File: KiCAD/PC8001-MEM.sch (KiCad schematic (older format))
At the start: 30 parts, among them J1 PC-8001 ext BUS, U1 74LS30, U10 74LS148, U11 628128, U2 74LS02, U3 74LS05, U4 74LS32, U5 74LS32, U6 74LS273, U7 74LS541, U8 74LS540, U9 74LS148

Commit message: README追加
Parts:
- removed C10, C11, C9: 0.1u, Capacitor_THT:C_Disc_D3.0mm_W1.6mm_P2.50mm, symbol Device:C
- removed R1, R2: 10k, symbol Device:R_US
- removed U1: 74LS30, symbol 74xx:74LS30
- removed U10, U9: 74LS148, symbol 74xx:74LS148
- removed U2: 74LS02, symbol 74xx:74LS02
- removed U3: 74LS05, symbol 74xx:74LS05
- removed U5: 74LS32, symbol 74xx:74LS32
- removed U8: 74LS540, symbol 74xx:74LS540
- added C? (x2): 0.1u, Capacitor_THT:C_Disc_D3.0mm_W1.6mm_P2.50mm, symbol Device:C
- added U? (x2): 74LS138, symbol 74xx:74LS138
- added U? (x3): 74LS74, symbol 74xx:74LS74
- added U? (x5): 74LS32, symbol 74xx:74LS32
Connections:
- net labels added: E2#RD, E2#WR, E3#RD, E3#WR, ~RAMRD, ~RAMWR
- net labels removed: 1MCS2, MA15, MA16, ~IOE2
- wire segments 345 -> 264
- no-connect marks 21 -> 25
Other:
- note added: "$010 - 02 : $E2 WR\n$100 - 04 : $E2 RD\n$011 - 03 : $E3 WR\n$101 - 05 : $E3 RD\n"
- note removed: "I/O E2h"
- moved on the sheet: C1, C12, C2, C3, C4, C5, C6, C7, C8, J1, MH1, MH2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

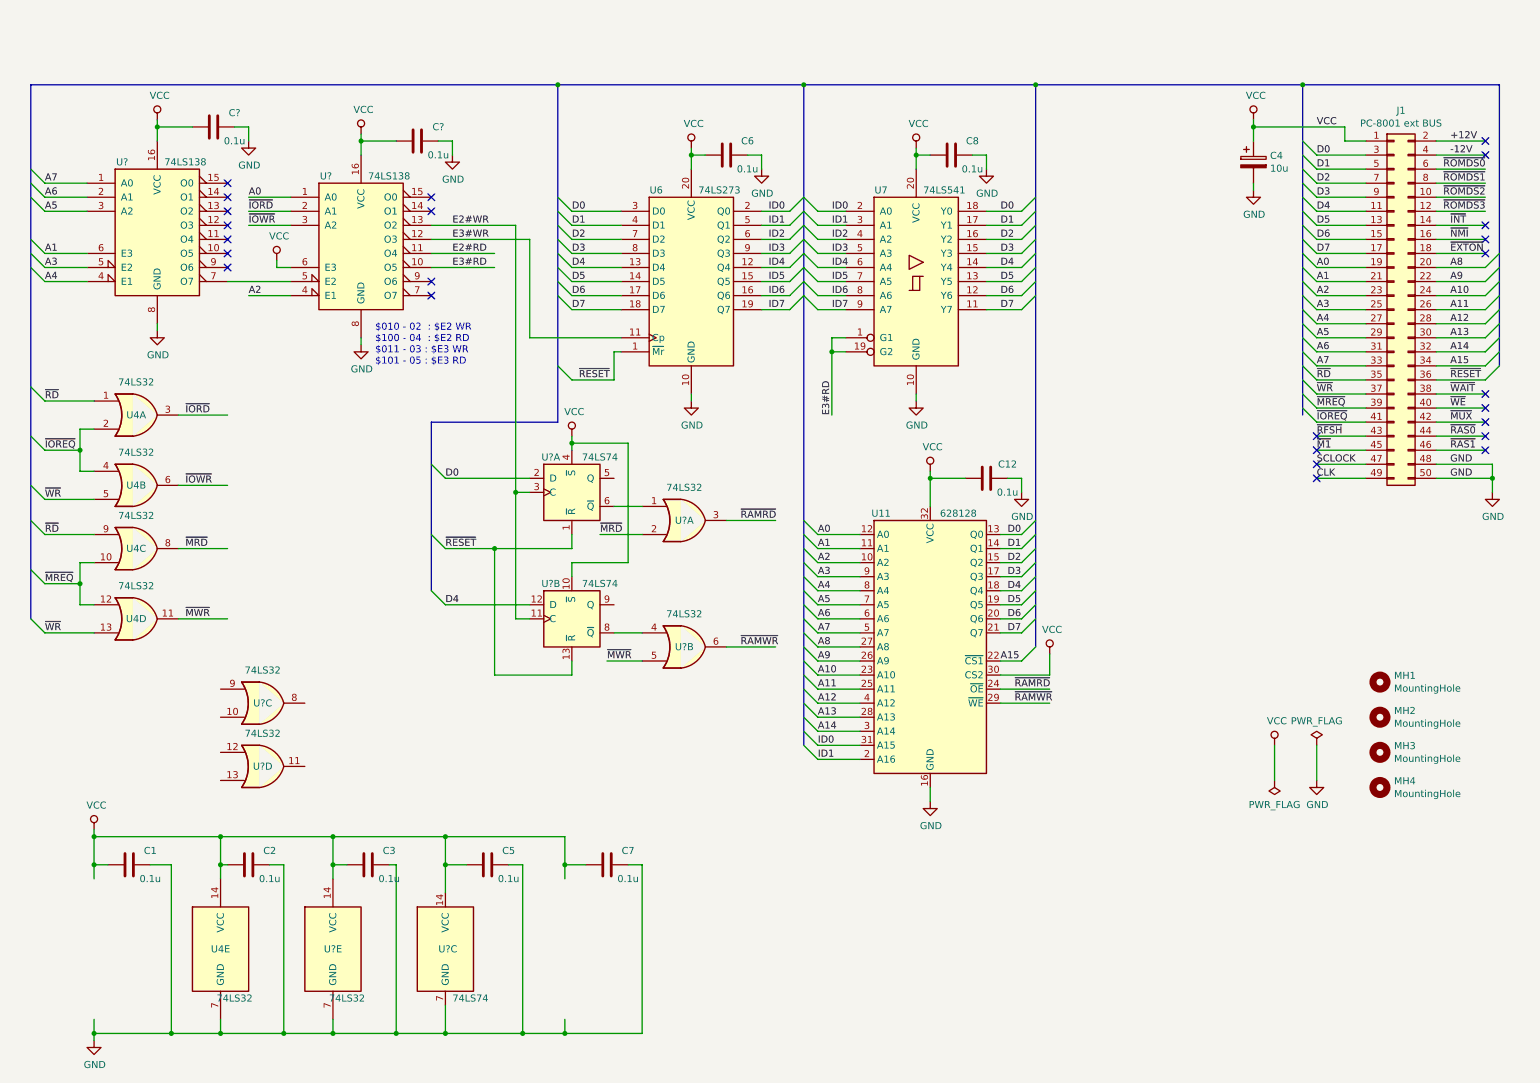
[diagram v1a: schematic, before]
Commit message: 回路図修正、イメージ追加
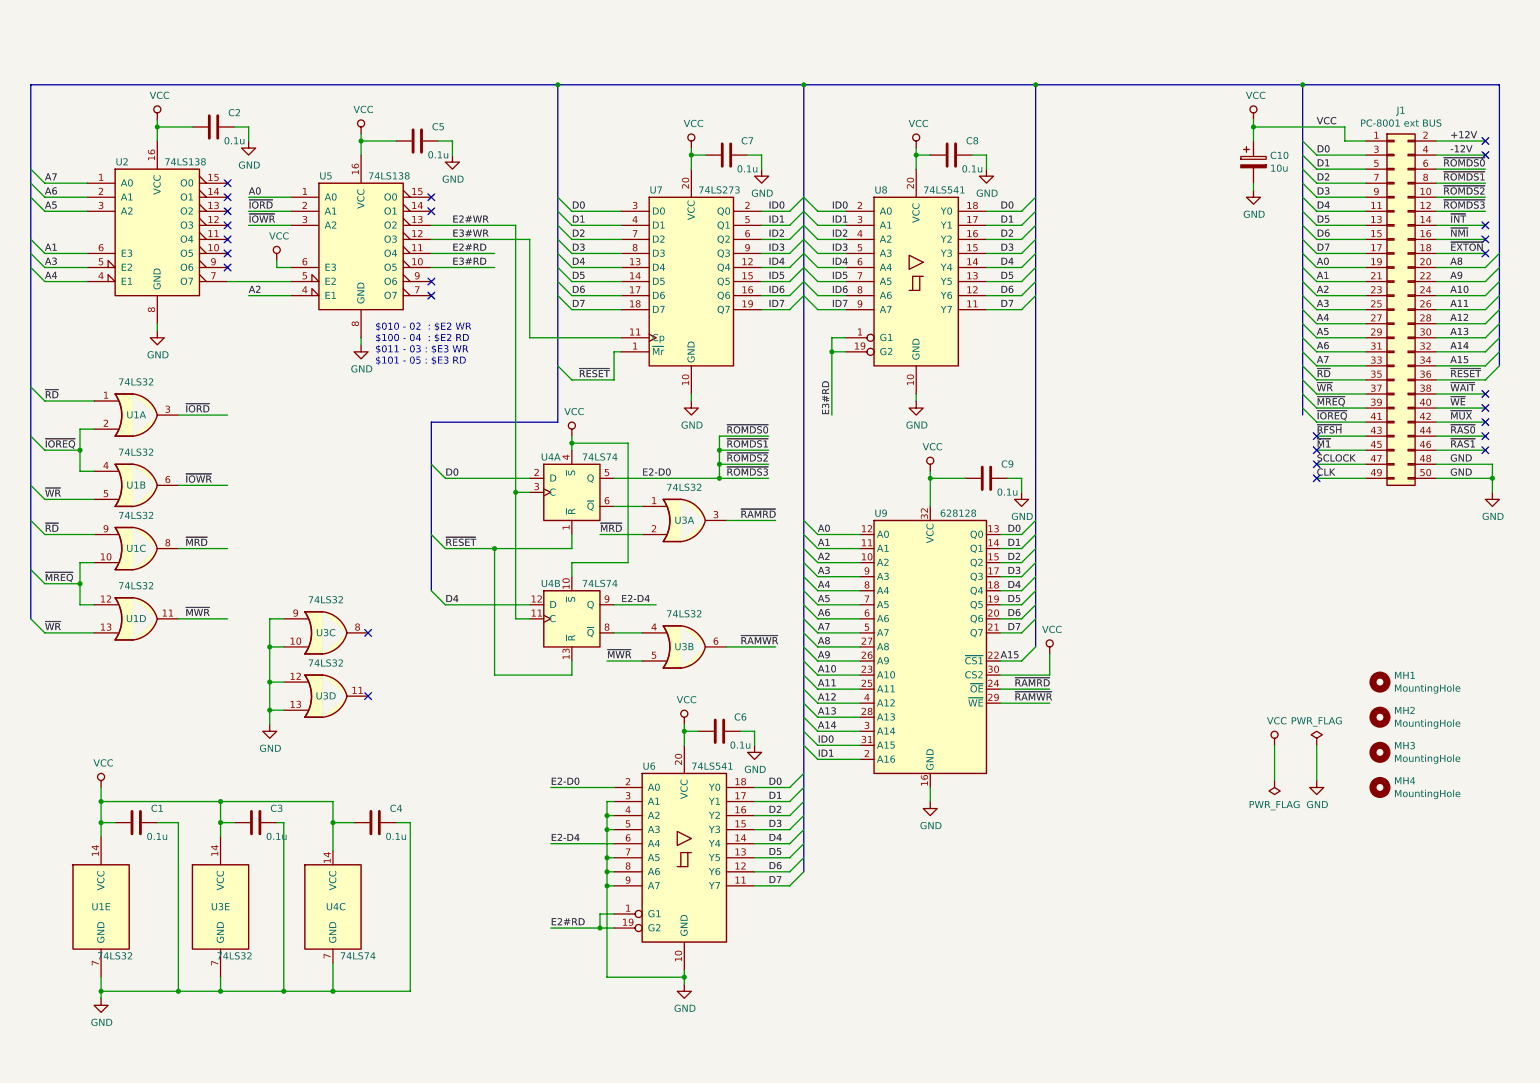
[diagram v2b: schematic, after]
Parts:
- removed C2, C7: 0.1u, Capacitor_THT:C_Disc_D3.0mm_W1.6mm_P2.50mm, symbol Device:C
- added C6: 0.1u, Capacitor_THT:C_Disc_D3.0mm_W1.6mm_P2.50mm, symbol Device:C
- added U6: 74LS541, symbol 74xx:74LS541
- gave numbers to parts that had none: 6
- renumbered C4 to C10, C5 to C4, C6 to C7, C12 to C9, U4 to U1, U6 to U7, U7 to U8, U11 to U9
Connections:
- net labels added: E2-D0, E2-D4
- wire segments 264 -> 297
- no-connect marks 25 -> 27
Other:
- moved on the sheet: C1, C3, C4, U1E, U3C, U3D, U3E, U4C

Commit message: アドレス E2用 LED追加
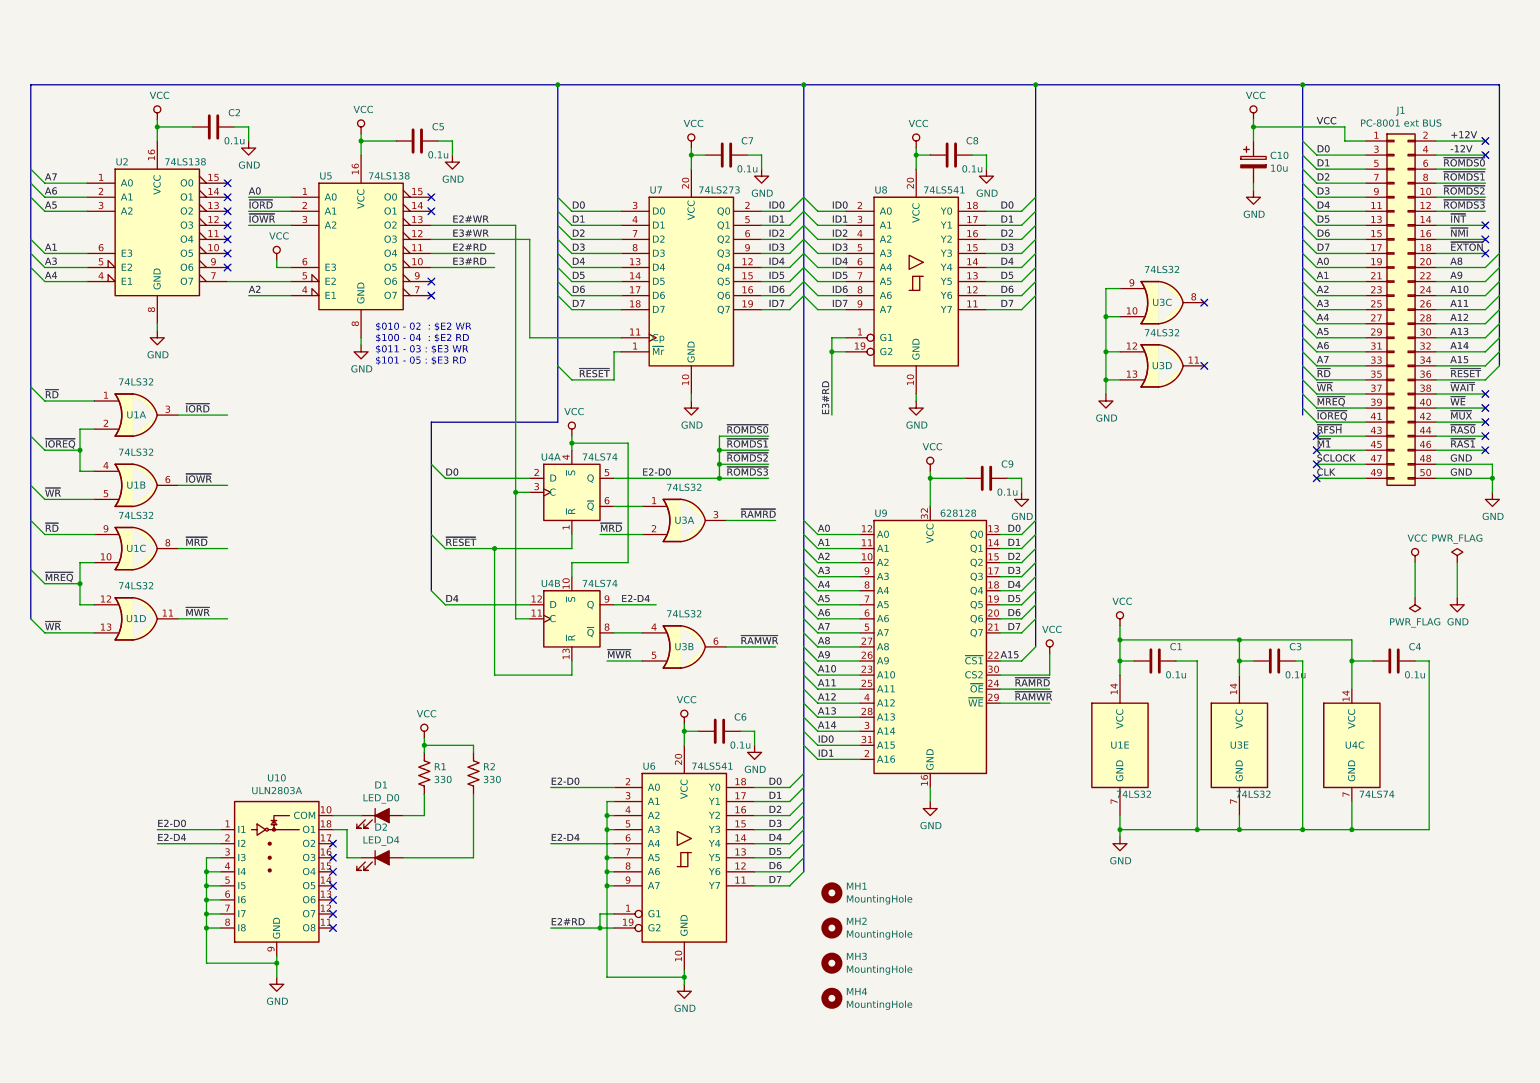
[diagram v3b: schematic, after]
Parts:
- added D1: LED_D0, symbol Device:LED_ALT
- added D2: LED_D4, symbol Device:LED_ALT
- added R1, R2: 330, symbol Device:R_US
- added U10: ULN2803A, symbol Transistor_Array:ULN2803A
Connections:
- wire segments 297 -> 326
- no-connect marks 27 -> 34
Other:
- moved on the sheet: C1, C3, C4, MH1, MH2, MH3, MH4, U1E, U3C, U3D, U3E, U4C

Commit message: 回路修正(ROM KILL間違い)
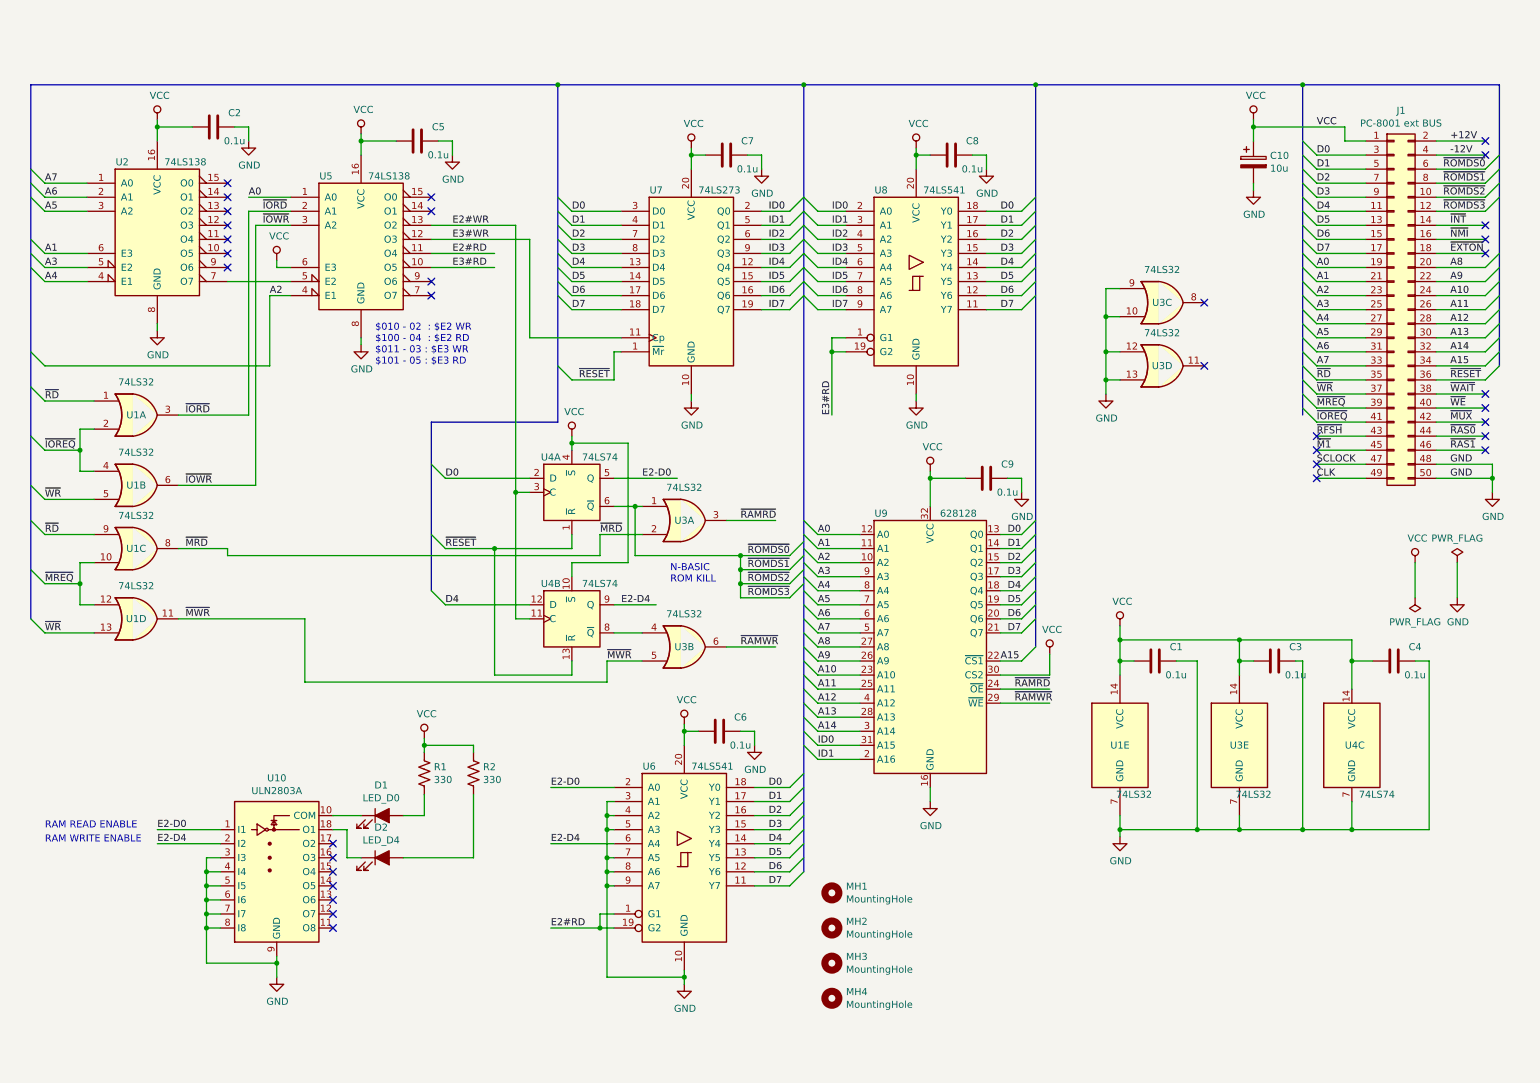
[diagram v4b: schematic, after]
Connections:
- wire segments 326 -> 339
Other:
- note added: "N-BASIC \nROM KILL"
- note added: "RAM READ ENABLE"
- note added: "RAM WRITE ENABLE"
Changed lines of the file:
@@
 Text Label 700  4900 0    50   ~ 0
 ~WR
-Wire Wire Line
-	1650 3350 2000 3350
 Text Label 1700 3350 0    50   ~ 0
 ~IORD
-Wire Wire Line
-	1650 3850 2000 3850
 Text Label 1700 3850 0    50   ~ 0
 ~IOWR
@@
 Text Label 1700 4300 0    50   ~ 0
 ~MRD
-Wire Wire Line
-	1650 4800 2000 4800
 Text Label 1700 4800 0    50   ~ 0
 ~MWR
@@
 Wire Wire Line
 	2150 1800 2450 1800
-Text Label 2150 1900 0    50   ~ 0
+Text Label 2250 1900 0    50   ~ 0
 ~IORD
 Wire Wire Line
-	2150 2000 2450 2000
-Text Label 2150 2000 0    50   ~ 0
+	2200 2000 2450 2000
+Text Label 2250 2000 0    50   ~ 0
 ~IOWR
 Wire Wire Line
@@
 	1    0    0    -1
 $EndComp
-Text Label 2150 2500 0    50   ~ 0
+Text Label 2300 2500 0    50   ~ 0
 A2
-Wire Wire Line
-	2150 2500 2450 2500
 NoConn ~ 3450 2500
 NoConn ~ 3450 2400
@@
 $EndComp
 Wire Wire Line
-	4750 4000 4950 4000
+	4750 4000 4900 4000
 Wire Wire Line
 	4750 4900 4950 4900
@@
 Connection ~ 9200 6300
 Wire Wire Line
-	5500 3500 5850 3500
-Wire Wire Line
-	5500 3600 5850 3600
-Wire Wire Line
-	5500 3700 5850 3700
-Text Label 5550 3500 0    50   ~ 0
+	5650 4350 6000 4350
+Wire Wire Line
+	5650 4450 6000 4450
+Wire Wire Line
+	5650 4550 6000 4550
+Text Label 5700 4350 0    50   ~ 0
 ~ROMDS0
-Text Label 5550 3600 0    50   ~ 0
+Text Label 5700 4450 0    50   ~ 0
 ~ROMDS1
-Text Label 5550 3700 0    50   ~ 0
+Text Label 5700 4550 0    50   ~ 0
 ~ROMDS2
-Text Label 5550 3800 0    50   ~ 0
+Text Label 5700 4650 0    50   ~ 0
 ~ROMDS3
 Wire Wire Line
-	4750 3800 5500 3800
-Wire Wire Line
-	5500 3800 5500 3700
-Connection ~ 5500 3800
-Wire Wire Line
-	5500 3800 5850 3800
-Connection ~ 5500 3600
-Wire Wire Line
-	5500 3600 5500 3500
-Connection ~ 5500 3700
-Wire Wire Line
-	5500 3700 5500 3600
+	5650 4650 5650 4550
+Wire Wire Line
+	5650 4650 6000 4650
+Connection ~ 5650 4450
+Wire Wire Line
+	5650 4450 5650 4350
+Connection ~ 5650 4550
+Wire Wire Line
+	5650 4550 5650 4450
 NoConn ~ 8950 2550
 NoConn ~ 8950 3000
@@
 Wire Wire Line
 	3750 6500 3250 6500
+Wire Wire Line
+	4900 4000 4900 4350
+Wire Wire Line
+	4900 4350 5650 4350
+Connection ~ 4900 4000
+Wire Wire Line
+	4900 4000 4950 4000
+Connection ~ 5650 4350
+Wire Wire Line
+	4750 3800 5200 3800
+Text Notes 5150 4550 0    50   ~ 0
+N-BASIC \nROM KILL
+Text Notes 700  6300 0    50   ~ 0
+RAM READ ENABLE
+Text Notes 700  6400 0    50   ~ 0
+RAM WRITE ENABLE
+Entry Wire Line
+	10950 1900 11050 1800
+Entry Wire Line
+	10950 1800 11050 1700
+Entry Wire Line
+	10950 1700 11050 1600
+Entry Wire Line
+	10950 1600 11050 1500
+Entry Wire Line
+	6000 4350 6100 4250
+Entry Wire Line
+	6000 4450 6100 4350
+Entry Wire Line
+	6000 4550 6100 4450
+Entry Wire Line
+	6000 4650 6100 4550
+Wire Wire Line
+	2550 4800 2550 5250
+Wire Wire Line
+	2550 5250 4700 5250
+Wire Wire Line
+	4700 5250 4700 5100
+Wire Wire Line
+	1650 4800 2550 4800
+Wire Wire Line
+	4650 4200 4650 4350
+Wire Wire Line
+	4650 4350 2000 4350
+Wire Wire Line
+	2000 4350 2000 4300
+Wire Wire Line
+	2200 2000 2200 3850
+Wire Wire Line
+	1650 3850 2200 3850
+Wire Wire Line
+	1650 3350 2150 3350
+Wire Wire Line
+	2150 1900 2150 3350
+Entry Wire Line
+	600  2900 700  3000
+Wire Wire Line
+	700  3000 2300 3000
+Wire Wire Line
+	2300 3000 2300 2500
+Wire Wire Line
+	2450 2500 2300 2500
 Wire Bus Line
 	3450 3400 3450 4600
@@
 	11050 1000 11050 3000
 Wire Bus Line
+	4350 1000 4350 3400
+Wire Bus Line
 	600  1000 600  4800
 Wire Bus Line
-	4350 1000 4350 3400
-Wire Bus Line
 	7750 1000 7750 5000
